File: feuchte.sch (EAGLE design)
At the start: 23 parts, among them CON1 CON_PCB_7.5MM_3-POLE, CON2 CON_PCB_7.5MM_3-POLE, IC1 IC_ULN2003AD, IC2 ESD_USB_IP4234CZ6, K1 RELAY_G5LA, K2 RELAY_G5LA, Q1 12MHz, U1 MCU_ATMEGA32U2-AU

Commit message: Weiter gelayouted
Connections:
- net USBCON_P renamed USBCON_
- net +5V: now also K1G$1.1, K2G$1.2; no longer K1G$1.2, K2G$1.1
- net N$11: now also IC1.I7; no longer IC1.I2
- net N$12: now also IC1.I2; no longer IC1.I7
- net N$13: now also K2G$1.1; no longer K1G$1.1
- net N$14: now also K1G$1.2; no longer K2G$1.2
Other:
- moved on the sheet: CON1, CON2, K1, K2
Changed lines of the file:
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@@
 <classes>
 <class number="0" name="default" width="0" drill="0">
+<clearance class="0" value="0.205"/>
 </class>
 </classes>
 <parts>
 <part name="U1" library="Bauelemente" deviceset="MCU_ATMEGA32U2-AU" device=""/>
-<part name="K1" library="Bauelemente" deviceset="RELAY_G5LA" device=""/>
+<part name="K2" library="Bauelemente" deviceset="RELAY_G5LA" device=""/>
 <part name="IC1" library="Bauelemente" deviceset="IC_ULN2003A" device="D"/>
 <part name="R1" library="Bauelemente" deviceset="R" device="" value="1k"/>
@@
 <part name="GND8" library="supply1" deviceset="GND" device=""/>
 <part name="P+5" library="supply1" deviceset="+5V" device=""/>
-<part name="K2" library="Bauelemente" deviceset="RELAY_G5LA" device=""/>
+<part name="K1" library="Bauelemente" deviceset="RELAY_G5LA" device=""/>
 <part name="P+6" library="supply1" deviceset="+5V" device=""/>
+<part name="CON2" library="Bauelemente" deviceset="CON_PCB_7.5MM_3-POLE" device=""/>
 <part name="CON1" library="Bauelemente" deviceset="CON_PCB_7.5MM_3-POLE" device=""/>
-<part name="CON2" library="Bauelemente" deviceset="CON_PCB_7.5MM_3-POLE" device=""/>
 </parts>
 <sheets>
@@
 <instances>
 <instance part="U1" gate="A" x="78.74" y="48.26"/>
-<instance part="K1" gate="G$1" x="167.64" y="78.74" rot="R180"/>
-<instance part="K1" gate="G$2" x="187.96" y="76.2"/>
+<instance part="K2" gate="G$1" x="167.64" y="78.74" rot="R180"/>
+<instance part="K2" gate="G$2" x="187.96" y="76.2"/>
 <instance part="IC1" gate="A" x="170.18" y="58.42"/>
 <instance part="R1" gate="G$1" x="170.18" y="27.94"/>
@@
 <instance part="GND8" gate="1" x="157.48" y="45.72"/>
 <instance part="P+5" gate="1" x="190.5" y="50.8"/>
-<instance part="K2" gate="G$1" x="203.2" y="78.74"/>
-<instance part="K2" gate="G$2" x="231.14" y="73.66"/>
+<instance part="K1" gate="G$1" x="203.2" y="78.74"/>
+<instance part="K1" gate="G$2" x="231.14" y="73.66"/>
 <instance part="P+6" gate="1" x="203.2" y="86.36"/>
-<instance part="CON1" gate="A" x="187.96" y="101.6" rot="MR270"/>
-<instance part="CON2" gate="A" x="231.14" y="101.6" rot="MR270"/>
+<instance part="CON2" gate="A" x="187.96" y="101.6" rot="MR270"/>
+<instance part="CON1" gate="A" x="231.14" y="101.6" rot="MR270"/>
 </instances>
 <busses>
@@
 </segment>
 </net>
-<net name="USBCON_P" class="0">
+<net name="USBCON_" class="0">
 <segment>
 <pinref part="USB1" gate="A" pin="D+"/>
@@
 </segment>
 <segment>
-<pinref part="K1" gate="G$1" pin="2"/>
+<pinref part="K2" gate="G$1" pin="2"/>
 <pinref part="P+4" gate="1" pin="+5V"/>
 </segment>
@@
 </segment>
 <segment>
-<pinref part="K2" gate="G$1" pin="1"/>
+<pinref part="K1" gate="G$1" pin="1"/>
 <pinref part="P+6" gate="1" pin="+5V"/>
 </segment>
@@
 </segment>
 </net>
-<net name="N$11" class="0">
-<segment>
-<wire x1="147.32" y1="45.72" x2="147.32" y2="63.5" width="0.1524" layer="91"/>
-<pinref part="U1" gate="A" pin="(OC1A)_PC6"/>
-<wire x1="147.32" y1="45.72" x2="106.68" y2="45.72" width="0.1524" layer="91"/>
-<pinref part="IC1" gate="A" pin="I2"/>
-<wire x1="147.32" y1="63.5" x2="157.48" y2="63.5" width="0.1524" layer="91"/>
-</segment>
-</net>
 <net name="N$13" class="0">
 <segment>
 <wire x1="187.96" y1="50.8" x2="187.96" y2="71.12" width="0.1524" layer="91"/>
 <wire x1="187.96" y1="71.12" x2="167.64" y2="71.12" width="0.1524" layer="91"/>
-<pinref part="K1" gate="G$1" pin="1"/>
+<pinref part="K2" gate="G$1" pin="1"/>
 <wire x1="167.64" y1="71.12" x2="167.64" y2="73.66" width="0.1524" layer="91"/>
 <pinref part="IC1" gate="A" pin="O7"/>
@@
 </segment>
 </net>
-<net name="N$12" class="0">
-<segment>
-<pinref part="U1" gate="A" pin="(OC0A/OC1C)_PB7"/>
-<wire x1="149.86" y1="55.88" x2="106.68" y2="55.88" width="0.1524" layer="91"/>
-<wire x1="106.68" y1="55.88" x2="106.68" y2="58.42" width="0.1524" layer="91"/>
-<pinref part="IC1" gate="A" pin="I7"/>
-<wire x1="157.48" y1="50.8" x2="149.86" y2="50.8" width="0.1524" layer="91"/>
-<wire x1="149.86" y1="50.8" x2="149.86" y2="55.88" width="0.1524" layer="91"/>
-</segment>
-</net>
 <net name="N$7" class="0">
+<segment>
+<pinref part="K2" gate="G$2" pin="P"/>
+<pinref part="CON2" gate="A" pin="2"/>
+<wire x1="187.96" y1="73.66" x2="187.96" y2="91.44" width="0.1524" layer="91"/>
+</segment>
+</net>
+<net name="N$15" class="0">
+<segment>
+<pinref part="K2" gate="G$2" pin="S"/>
+<pinref part="CON2" gate="A" pin="1"/>
+<wire x1="182.88" y1="81.28" x2="185.42" y2="81.28" width="0.1524" layer="91"/>
+<wire x1="185.42" y1="81.28" x2="185.42" y2="91.44" width="0.1524" layer="91"/>
+</segment>
+</net>
+<net name="N$16" class="0">
+<segment>
+<pinref part="K2" gate="G$2" pin="O"/>
+<pinref part="CON2" gate="A" pin="3"/>
+<wire x1="193.04" y1="81.28" x2="190.5" y2="81.28" width="0.1524" layer="91"/>
+<wire x1="190.5" y1="81.28" x2="190.5" y2="91.44" width="0.1524" layer="91"/>
+</segment>
+</net>
+<net name="N$17" class="0">
+<segment>
+<pinref part="K1" gate="G$2" pin="S"/>
+<pinref part="CON1" gate="A" pin="1"/>
+<wire x1="226.06" y1="78.74" x2="228.6" y2="78.74" width="0.1524" layer="91"/>
+<wire x1="228.6" y1="78.74" x2="228.6" y2="91.44" width="0.1524" layer="91"/>
+</segment>
+</net>
+<net name="N$18" class="0">
 <segment>
 <pinref part="K1" gate="G$2" pin="P"/>
 <pinref part="CON1" gate="A" pin="2"/>
-<wire x1="187.96" y1="73.66" x2="187.96" y2="91.44" width="0.1524" layer="91"/>
-</segment>
-</net>
-<net name="N$15" class="0">
-<segment>
-<pinref part="K1" gate="G$2" pin="S"/>
-<pinref part="CON1" gate="A" pin="1"/>
-<wire x1="182.88" y1="81.28" x2="185.42" y2="81.28" width="0.1524" layer="91"/>
-<wire x1="185.42" y1="81.28" x2="185.42" y2="91.44" width="0.1524" layer="91"/>
-</segment>
-</net>
-<net name="N$16" class="0">
+<wire x1="231.14" y1="71.12" x2="231.14" y2="91.44" width="0.1524" layer="91"/>
+</segment>
+</net>
+<net name="N$19" class="0">
 <segment>
 <pinref part="K1" gate="G$2" pin="O"/>
 <pinref part="CON1" gate="A" pin="3"/>
-<wire x1="193.04" y1="81.28" x2="190.5" y2="81.28" width="0.1524" layer="91"/>
-<wire x1="190.5" y1="81.28" x2="190.5" y2="91.44" width="0.1524" layer="91"/>
-</segment>
-</net>
-<net name="N$17" class="0">
-<segment>
-<pinref part="K2" gate="G$2" pin="S"/>
-<pinref part="CON2" gate="A" pin="1"/>
-<wire x1="226.06" y1="78.74" x2="228.6" y2="78.74" width="0.1524" layer="91"/>
-<wire x1="228.6" y1="78.74" x2="228.6" y2="91.44" width="0.1524" layer="91"/>
-</segment>
-</net>
-<net name="N$18" class="0">
-<segment>
-<pinref part="K2" gate="G$2" pin="P"/>
-<pinref part="CON2" gate="A" pin="2"/>
-<wire x1="231.14" y1="71.12" x2="231.14" y2="91.44" width="0.1524" layer="91"/>
-</segment>
-</net>
-<net name="N$19" class="0">
-<segment>
-<pinref part="K2" gate="G$2" pin="O"/>
-<pinref part="CON2" gate="A" pin="3"/>
 <wire x1="236.22" y1="78.74" x2="233.68" y2="78.74" width="0.1524" layer="91"/>
 <wire x1="233.68" y1="78.74" x2="233.68" y2="91.44" width="0.1524" layer="91"/>
@@
 <segment>
 <pinref part="IC1" gate="A" pin="O2"/>
-<pinref part="K2" gate="G$1" pin="2"/>
+<pinref part="K1" gate="G$1" pin="2"/>
 <wire x1="182.88" y1="63.5" x2="203.2" y2="63.5" width="0.1524" layer="91"/>
 <wire x1="203.2" y1="63.5" x2="203.2" y2="73.66" width="0.1524" layer="91"/>
 </segment>
 </net>
+<net name="N$11" class="0">
+<segment>
+<pinref part="U1" gate="A" pin="(OC1A)_PC6"/>
+<wire x1="106.68" y1="45.72" x2="149.86" y2="45.72" width="0.1524" layer="91"/>
+<wire x1="149.86" y1="45.72" x2="149.86" y2="50.8" width="0.1524" layer="91"/>
+<pinref part="IC1" gate="A" pin="I7"/>
+<wire x1="149.86" y1="50.8" x2="157.48" y2="50.8" width="0.1524" layer="91"/>
+</segment>
+</net>
+<net name="N$12" class="0">
+<segment>
+<pinref part="U1" gate="A" pin="(OC0A/OC1C)_PB7"/>
+<wire x1="106.68" y1="58.42" x2="114.3" y2="58.42" width="0.1524" layer="91"/>
+<wire x1="114.3" y1="58.42" x2="114.3" y2="53.34" width="0.1524" layer="91"/>
+<wire x1="114.3" y1="53.34" x2="149.86" y2="53.34" width="0.1524" layer="91"/>
+<wire x1="149.86" y1="53.34" x2="149.86" y2="63.5" width="0.1524" layer="91"/>
+<pinref part="IC1" gate="A" pin="I2"/>
+<wire x1="149.86" y1="63.5" x2="157.48" y2="63.5" width="0.1524" layer="91"/>
+</segment>
+</net>

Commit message: weiter gelayouted
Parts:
- added R4: 1k, Bauelemente:R
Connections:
- net USBC_N renamed USBC_
- net USBR_N renamed USBR_
- new net N$20: R4.2, U1.(!HWB!/T0/!CTS!/AIN6)_PD7
- net GND: now also IC1.I1, IC1.I3, IC1.I4, IC1.I5, IC1.I6, R4.1; no longer U1.(!HWB!/T0/!CTS!/AIN6)_PD7
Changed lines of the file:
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@@
 <part name="CON2" library="Bauelemente" deviceset="CON_PCB_7.5MM_3-POLE" device=""/>
 <part name="CON1" library="Bauelemente" deviceset="CON_PCB_7.5MM_3-POLE" device=""/>
+<part name="R4" library="Bauelemente" deviceset="R" device="" value="1k"/>
 </parts>
 <sheets>
@@
 <instance part="GND4" gate="1" x="43.18" y="58.42"/>
 <instance part="GND5" gate="1" x="22.86" y="66.04"/>
-<instance part="GND6" gate="1" x="106.68" y="17.78"/>
+<instance part="GND6" gate="1" x="106.68" y="7.62"/>
 <instance part="U$1" gate="1" x="132.08" y="71.12" rot="MR0"/>
 <instance part="P+3" gate="1" x="121.92" y="78.74"/>
@@
 <instance part="CON2" gate="A" x="187.96" y="101.6" rot="MR270"/>
 <instance part="CON1" gate="A" x="231.14" y="101.6" rot="MR270"/>
+<instance part="R4" gate="G$1" x="106.68" y="15.24" rot="R90"/>
 </instances>
 <busses>
@@
 </segment>
 <segment>
-<pinref part="U1" gate="A" pin="(!HWB!/T0/!CTS!/AIN6)_PD7"/>
-<pinref part="GND6" gate="1" pin="GND"/>
-</segment>
-<segment>
 <pinref part="U$1" gate="1" pin="GND"/>
 <pinref part="GND7" gate="1" pin="GND"/>
@@
 <pinref part="IC1" gate="A" pin="GND"/>
 <pinref part="GND8" gate="1" pin="GND"/>
+<wire x1="157.48" y1="48.26" x2="154.94" y2="48.26" width="0.1524" layer="91"/>
+<junction x="157.48" y="48.26"/>
+<wire x1="154.94" y1="48.26" x2="154.94" y2="53.34" width="0.1524" layer="91"/>
+<pinref part="IC1" gate="A" pin="I6"/>
+<pinref part="IC1" gate="A" pin="I5"/>
+<wire x1="157.48" y1="53.34" x2="157.48" y2="55.88" width="0.1524" layer="91"/>
+<pinref part="IC1" gate="A" pin="I4"/>
+<wire x1="157.48" y1="55.88" x2="157.48" y2="58.42" width="0.1524" layer="91"/>
+<junction x="157.48" y="55.88"/>
+<pinref part="IC1" gate="A" pin="I3"/>
+<wire x1="157.48" y1="58.42" x2="157.48" y2="60.96" width="0.1524" layer="91"/>
+<junction x="157.48" y="58.42"/>
+<wire x1="154.94" y1="53.34" x2="157.48" y2="53.34" width="0.1524" layer="91"/>
+<junction x="157.48" y="53.34"/>
+<wire x1="157.48" y1="60.96" x2="154.94" y2="60.96" width="0.1524" layer="91"/>
+<junction x="157.48" y="60.96"/>
+<wire x1="154.94" y1="60.96" x2="154.94" y2="66.04" width="0.1524" layer="91"/>
+<pinref part="IC1" gate="A" pin="I1"/>
+<wire x1="154.94" y1="66.04" x2="157.48" y2="66.04" width="0.1524" layer="91"/>
+</segment>
+<segment>
+<pinref part="GND6" gate="1" pin="GND"/>
+<pinref part="R4" gate="G$1" pin="1"/>
 </segment>
 </net>
@@
 </segment>
 </net>
-<net name="USBC_N" class="0">
+<net name="USBC_" class="0">
 <segment>
 <pinref part="U1" gate="A" pin="D-"/>
@@
 </segment>
 </net>
-<net name="USBR_N" class="0">
+<net name="USBR_" class="0">
 <segment>
 <pinref part="IC2" gate="A" pin="D-µC"/>
@@
 <pinref part="U1" gate="A" pin="!RESET!_(PC1/DW)"/>
 <wire x1="50.8" y1="33.02" x2="45.72" y2="33.02" width="0.1524" layer="91"/>
-<wire x1="45.72" y1="33.02" x2="45.72" y2="10.16" width="0.1524" layer="91"/>
-<wire x1="45.72" y1="10.16" x2="116.84" y2="10.16" width="0.1524" layer="91"/>
-<wire x1="116.84" y1="10.16" x2="116.84" y2="66.04" width="0.1524" layer="91"/>
+<wire x1="45.72" y1="33.02" x2="45.72" y2="5.08" width="0.1524" layer="91"/>
+<wire x1="45.72" y1="5.08" x2="116.84" y2="5.08" width="0.1524" layer="91"/>
+<wire x1="116.84" y1="5.08" x2="116.84" y2="66.04" width="0.1524" layer="91"/>
 <pinref part="U$1" gate="1" pin="RESET"/>
 <wire x1="116.84" y1="66.04" x2="121.92" y2="66.04" width="0.1524" layer="91"/>
@@
 </segment>
 </net>
+<net name="N$20" class="0">
+<segment>
+<pinref part="U1" gate="A" pin="(!HWB!/T0/!CTS!/AIN6)_PD7"/>
+<pinref part="R4" gate="G$1" pin="2"/>
+</segment>
+</net>

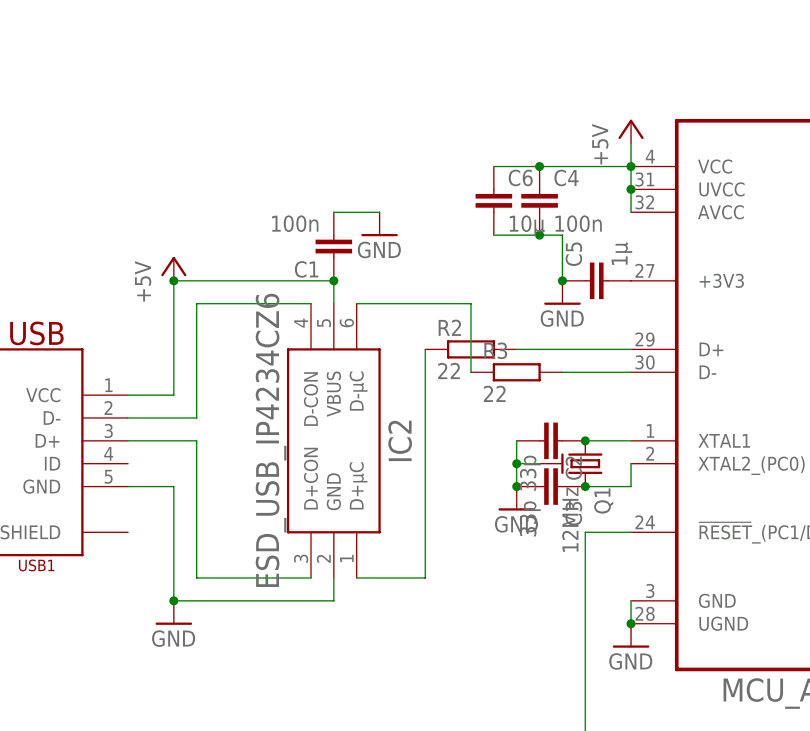
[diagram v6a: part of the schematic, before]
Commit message: weiter gelayouted, jetzt mit quarz
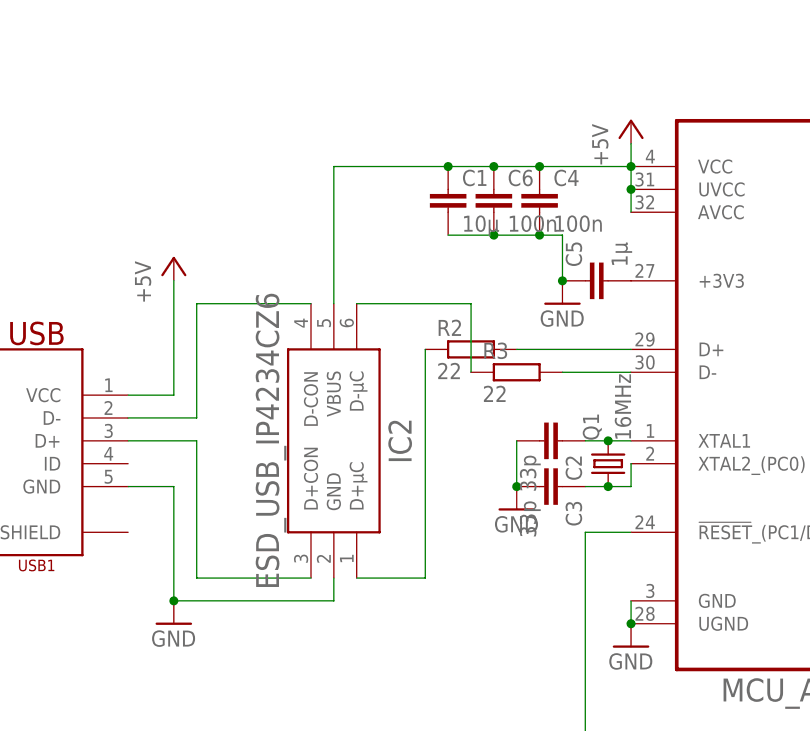
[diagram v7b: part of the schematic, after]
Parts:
- C1: value 100n -> 10µ
- C6: value 10µ -> 100n
- Q1: value 12MHz -> 16MHz; device Bauelemente:QUARTZ_ABMM2 -> Bauelemente:QUARTZ_HC49S
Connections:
- net GND: no longer Q1.GND
- net N$1: now also Q1.2; no longer Q1.1
- net N$2: now also Q1.1; no longer Q1.2
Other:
- moved on the sheet: C1
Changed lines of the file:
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@@
 <part name="IC1" library="Bauelemente" deviceset="IC_ULN2003A" device="D"/>
 <part name="R1" library="Bauelemente" deviceset="R" device="" value="1k"/>
-<part name="C1" library="Bauelemente" deviceset="C" device="" value="100n"/>
-<part name="Q1" library="Bauelemente" deviceset="QUARTZ_ABMM2" device="" value="12MHz"/>
+<part name="C1" library="Bauelemente" deviceset="C" device="" value="10µ"/>
 <part name="C2" library="Bauelemente" deviceset="C" device="" value="33p"/>
 <part name="C3" library="Bauelemente" deviceset="C" device="" value="33p"/>
 <part name="C4" library="Bauelemente" deviceset="C" device="" value="100n"/>
 <part name="C5" library="Bauelemente" deviceset="C" device="" value="1µ"/>
-<part name="C6" library="Bauelemente" deviceset="C" device="" value="10µ"/>
+<part name="C6" library="Bauelemente" deviceset="C" device="" value="100n"/>
 <part name="R2" library="Bauelemente" deviceset="R" device="" value="22"/>
 <part name="R3" library="Bauelemente" deviceset="R" device="" value="22"/>
@@
 <part name="GND3" library="supply1" deviceset="GND" device=""/>
 <part name="GND4" library="supply1" deviceset="GND" device=""/>
-<part name="GND5" library="supply1" deviceset="GND" device=""/>
 <part name="GND6" library="supply1" deviceset="GND" device=""/>
 <part name="U$1" library="Bauelemente" deviceset="CON_SPI_AVR10" device=""/>
@@
 <part name="CON1" library="Bauelemente" deviceset="CON_PCB_7.5MM_3-POLE" device=""/>
 <part name="R4" library="Bauelemente" deviceset="R" device="" value="1k"/>
+<part name="Q1" library="Bauelemente" deviceset="QUARTZ_HC49S" device="" value="16MHz"/>
 </parts>
 <sheets>
@@
 <instance part="IC1" gate="A" x="170.18" y="58.42"/>
 <instance part="R1" gate="G$1" x="170.18" y="27.94"/>
-<instance part="C1" gate="G$1" x="17.78" y="63.5" rot="R180"/>
-<instance part="Q1" gate="G$1" x="45.72" y="40.64" rot="R270"/>
+<instance part="C1" gate="G$1" x="30.48" y="71.12"/>
 <instance part="C2" gate="G$1" x="43.18" y="43.18" rot="R270"/>
 <instance part="C3" gate="G$1" x="43.18" y="38.1" rot="R270"/>
@@
 <instance part="GND3" gate="1" x="38.1" y="35.56"/>
 <instance part="GND4" gate="1" x="43.18" y="58.42"/>
-<instance part="GND5" gate="1" x="22.86" y="66.04"/>
 <instance part="GND6" gate="1" x="106.68" y="7.62"/>
 <instance part="U$1" gate="1" x="132.08" y="71.12" rot="MR0"/>
@@
 <instance part="CON1" gate="A" x="231.14" y="101.6" rot="MR270"/>
 <instance part="R4" gate="G$1" x="106.68" y="15.24" rot="R90"/>
+<instance part="Q1" gate="A" x="48.26" y="40.64" rot="R90"/>
 </instances>
 <busses>
@@
 <net name="N$1" class="0">
 <segment>
-<pinref part="Q1" gate="G$1" pin="1"/>
 <pinref part="C2" gate="G$1" pin="1"/>
 <pinref part="U1" gate="A" pin="XTAL1"/>
-<wire x1="45.72" y1="43.18" x2="50.8" y2="43.18" width="0.1524" layer="91"/>
-<junction x="45.72" y="43.18"/>
+<wire x1="45.72" y1="43.18" x2="48.26" y2="43.18" width="0.1524" layer="91"/>
+<pinref part="Q1" gate="A" pin="2"/>
+<wire x1="48.26" y1="43.18" x2="50.8" y2="43.18" width="0.1524" layer="91"/>
+<junction x="48.26" y="43.18"/>
 </segment>
 </net>
 <net name="N$2" class="0">
 <segment>
-<pinref part="Q1" gate="G$1" pin="2"/>
 <pinref part="C3" gate="G$1" pin="1"/>
 <pinref part="U1" gate="A" pin="XTAL2_(PC0)"/>
 <wire x1="50.8" y1="40.64" x2="50.8" y2="38.1" width="0.1524" layer="91"/>
-<wire x1="50.8" y1="38.1" x2="45.72" y2="38.1" width="0.1524" layer="91"/>
-<junction x="45.72" y="38.1"/>
+<wire x1="50.8" y1="38.1" x2="48.26" y2="38.1" width="0.1524" layer="91"/>
+<pinref part="Q1" gate="A" pin="1"/>
+<wire x1="48.26" y1="38.1" x2="45.72" y2="38.1" width="0.1524" layer="91"/>
+<junction x="48.26" y="38.1"/>
 </segment>
 </net>
@@
 <pinref part="C2" gate="G$1" pin="2"/>
 <pinref part="C3" gate="G$1" pin="2"/>
-<wire x1="38.1" y1="43.18" x2="38.1" y2="40.64" width="0.1524" layer="91"/>
 <pinref part="GND3" gate="1" pin="GND"/>
 <junction x="38.1" y="38.1"/>
-<pinref part="Q1" gate="G$1" pin="GND"/>
-<wire x1="38.1" y1="40.64" x2="38.1" y2="38.1" width="0.1524" layer="91"/>
-<wire x1="40.64" y1="40.64" x2="38.1" y2="40.64" width="0.1524" layer="91"/>
-<junction x="38.1" y="40.64"/>
+<wire x1="38.1" y1="43.18" x2="38.1" y2="38.1" width="0.1524" layer="91"/>
 </segment>
 <segment>
@@
 <pinref part="C4" gate="G$1" pin="2"/>
 <junction x="40.64" y="66.04"/>
-</segment>
-<segment>
 <pinref part="C1" gate="G$1" pin="2"/>
-<pinref part="GND5" gate="1" pin="GND"/>
-<wire x1="17.78" y1="68.58" x2="22.86" y2="68.58" width="0.1524" layer="91"/>
+<wire x1="30.48" y1="66.04" x2="35.56" y2="66.04" width="0.1524" layer="91"/>
+<junction x="35.56" y="66.04"/>
 </segment>
 <segment>
@@
 <net name="+5V" class="0">
 <segment>
-<wire x1="17.78" y1="58.42" x2="17.78" y2="60.96" width="0.1524" layer="91"/>
-<wire x1="17.78" y1="60.96" x2="0" y2="60.96" width="0.1524" layer="91"/>
 <wire x1="0" y1="60.96" x2="0" y2="48.26" width="0.1524" layer="91"/>
 <pinref part="USB1" gate="A" pin="VCC"/>
 <wire x1="0" y1="48.26" x2="-5.08" y2="48.26" width="0.1524" layer="91"/>
-<pinref part="IC2" gate="A" pin="VBUS"/>
 <pinref part="P+1" gate="1" pin="+5V"/>
-<junction x="0" y="60.96"/>
-<pinref part="C1" gate="G$1" pin="1"/>
-<junction x="17.78" y="60.96"/>
 </segment>
 <segment>
@@
 <junction x="40.64" y="73.66"/>
 <wire x1="40.64" y1="73.66" x2="50.8" y2="73.66" width="0.1524" layer="91"/>
-</segment>
-<segment>
+<pinref part="C1" gate="G$1" pin="1"/>
+<wire x1="35.56" y1="73.66" x2="30.48" y2="73.66" width="0.1524" layer="91"/>
+<junction x="35.56" y="73.66"/>
+<pinref part="IC2" gate="A" pin="VBUS"/>
+<wire x1="30.48" y1="73.66" x2="17.78" y2="73.66" width="0.1524" layer="91"/>
+<wire x1="17.78" y1="73.66" x2="17.78" y2="58.42" width="0.1524" layer="91"/>
+<junction x="30.48" y="73.66"/>
+</segment>
+<segment>
